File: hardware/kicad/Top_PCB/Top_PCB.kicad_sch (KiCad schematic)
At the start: 3 parts, among them J1 XT30PW-M

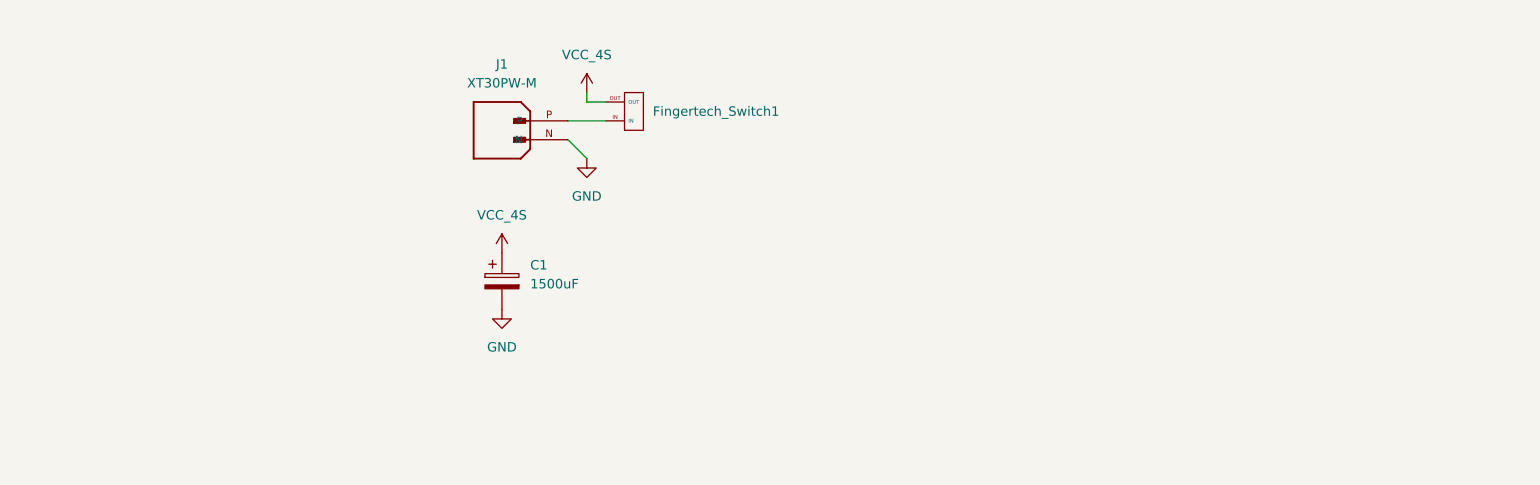
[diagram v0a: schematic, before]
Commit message: Did some top board work (added regulator), added vias and refined geometry a bit
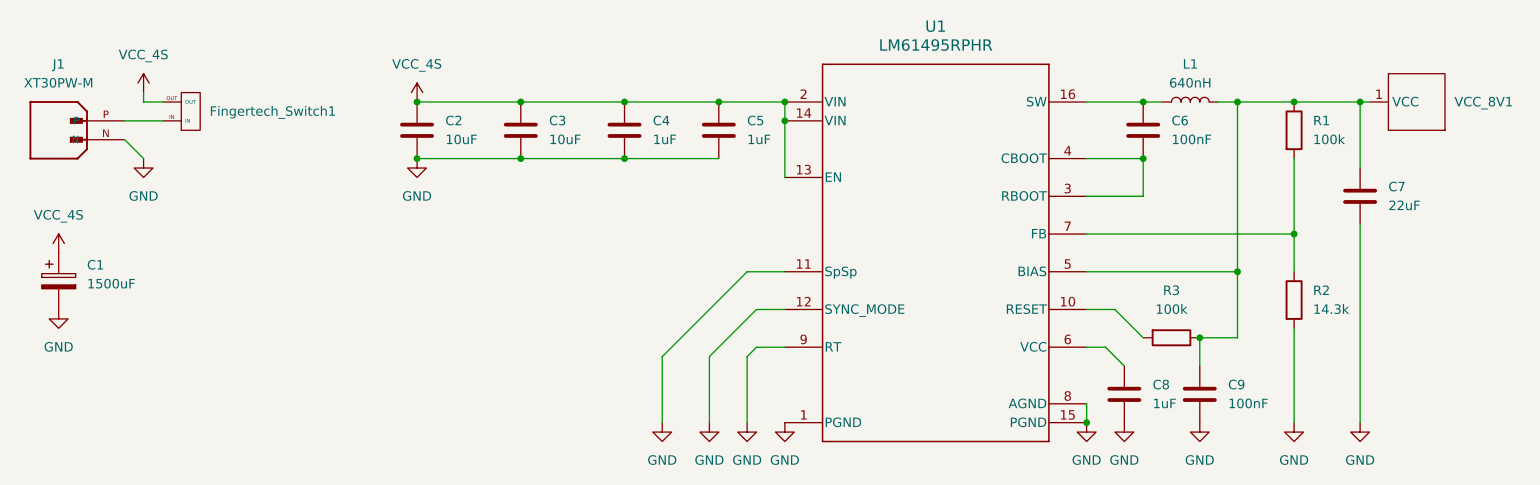
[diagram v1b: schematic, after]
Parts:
- added C2, C3: 10uF, Capacitor_SMD:C_1206_3216Metric_Pad1.33x1.80mm_HandSolder, symbol Device:C
- added C4, C5, C8: 1uF, Capacitor_SMD:C_1206_3216Metric_Pad1.33x1.80mm_HandSolder, symbol Device:C
- added C6, C9: 100nF, Capacitor_SMD:C_1206_3216Metric_Pad1.33x1.80mm_HandSolder, symbol Device:C
- added C7: 22uF, Capacitor_SMD:C_1206_3216Metric_Pad1.33x1.80mm_HandSolder, symbol Device:C
- added L1: 640nH, Inductor_SMD:L_1206_3216Metric_Pad1.22x1.90mm_HandSolder, symbol Device:L
- added R1, R3: 100k, PCB-V2-Footprints:R_1206_3216Metric_Pad1.30x1.75mm_HandSolder, symbol PCB-V2-Symbols:R
- added R2: 14.3k, PCB-V2-Footprints:R_1206_3216Metric_Pad1.30x1.75mm_HandSolder, symbol PCB-V2-Symbols:R
- added U1: LM61495RPHR, RPH0016A, symbol LM61495RPH:LM61495RPHR
- added VCC_8V1: (no value), Pads:VCC_Standalone, symbol Pads:VCC_Standalone
- J1: footprint XT-30 Horizontal:AMASS_XT30PW-M -> AMASS_XT30PW-M:AMASS_XT30PW-M
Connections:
- net GND: now also C2.2, C3.2, C4.2, C5.2, C7.2, C8.2, C9.2, R2.2, U1.1 (PGND), U1.11 (SpSp), U1.12 (SYNC_MODE), U1.15 (PGND), U1.8 (AGND), U1.9 (RT)
- net VCC_4S: now also C2.1, C3.1, C4.1, C5.1, U1.13 (EN), U1.14 (VIN), U1.2 (VIN)
- new net: C6.1, L1.1, U1.16 (SW)
- new net: C6.2, U1.3 (RBOOT), U1.4 (CBOOT)
- new net: R1.2, R2.1, U1.7 (FB)
- new net: R3.2, U1.10 (RESET)
- new net: C7.1, C9.1, L1.2, R1.1, R3.1, U1.5 (BIAS), VCC_8V1.1 (VCC)
- new net: C8.1, U1.6 (VCC)
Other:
- moved on the sheet: C1, Fingertech_Switch1, J1
